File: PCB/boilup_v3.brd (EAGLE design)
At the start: 59.7 x 50.8 mm, 50 parts, among them U1 STM32F0_LQFP64, U2 SPX3819-3.3

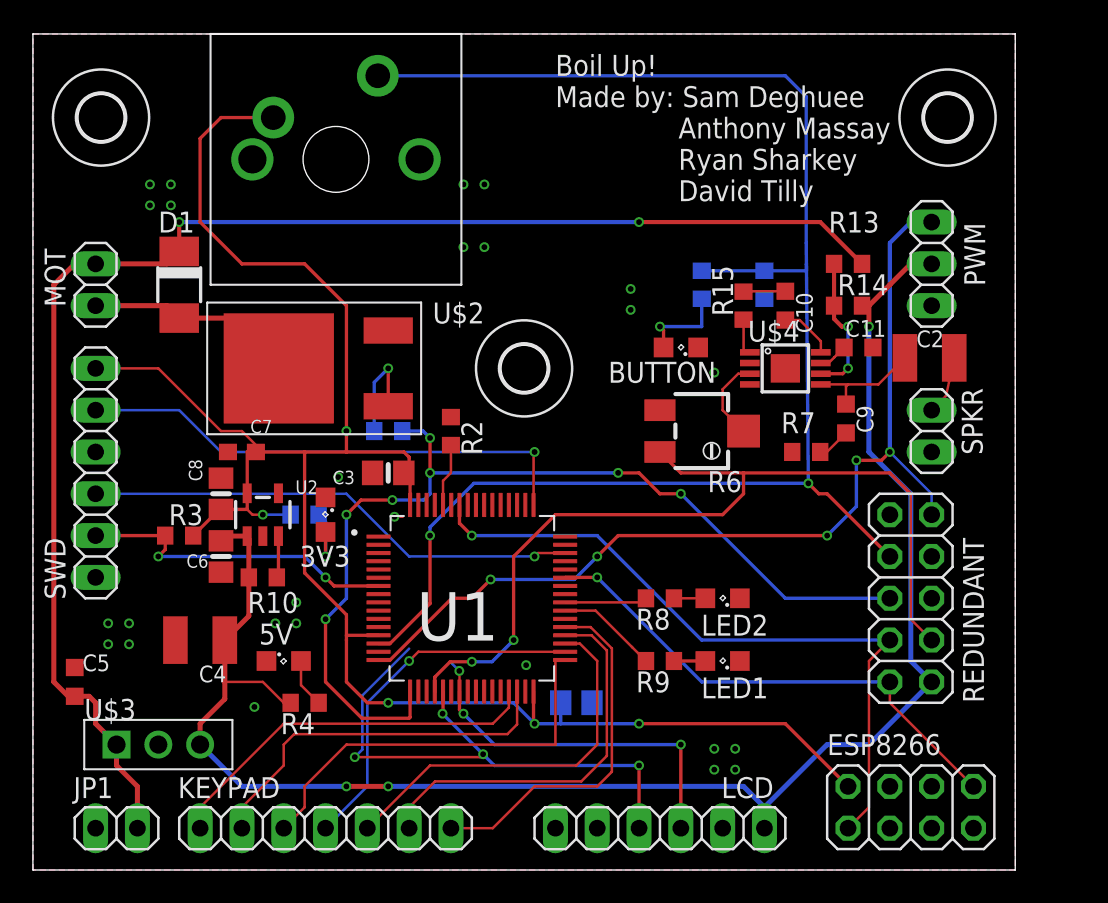
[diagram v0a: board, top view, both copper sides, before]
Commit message: v3 using i2c and a level shifter
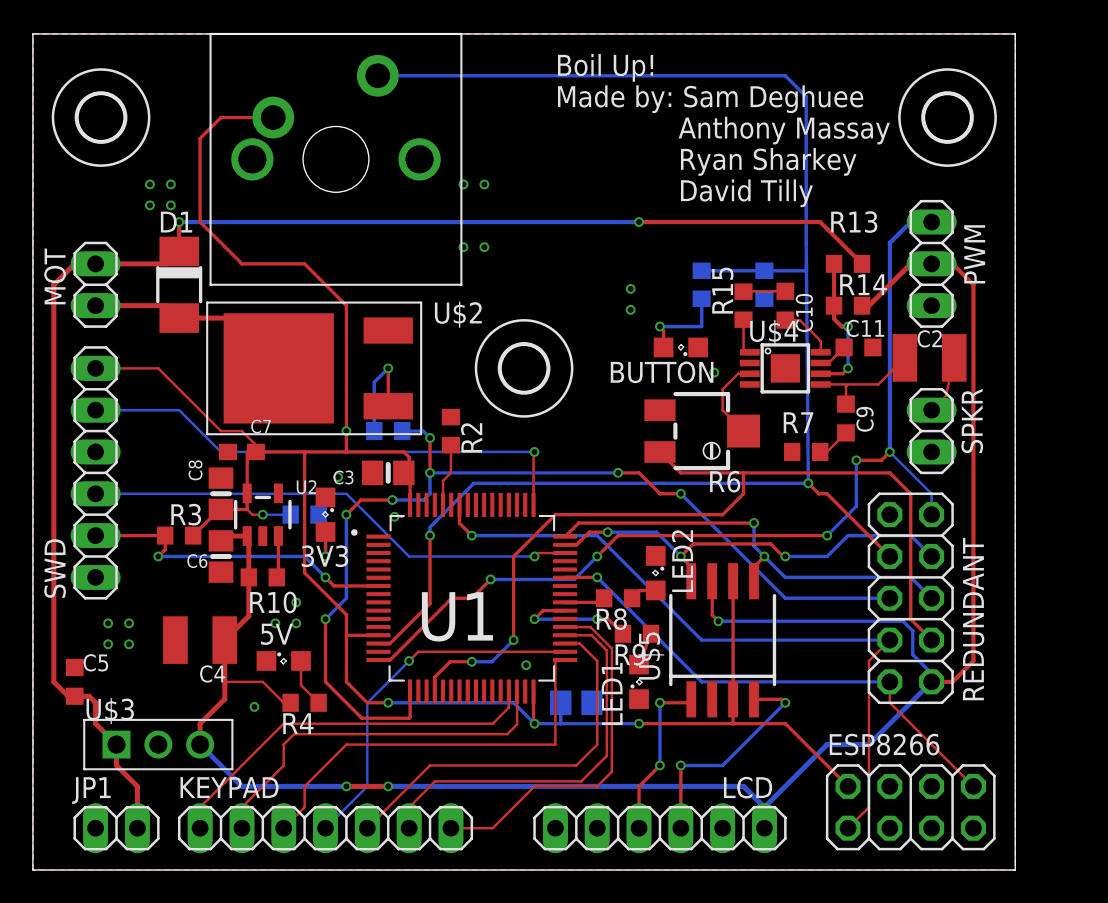
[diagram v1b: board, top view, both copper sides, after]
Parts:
- added U$5: TXS0102, smarttle:SOP-08
- moved LED1 5.24 mm to (36.8, 11.4), turned to 90 degrees
- moved LED2 4.34 mm to (37.8, 18.0), turned to 270 degrees
- moved R8 2.54 mm to (35.6, 16.5)
- moved R9 2.16 mm to (36.7, 14.4)
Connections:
- removed net MISO: U1.22
- removed net MOSI: LCD.4, U1.23
- removed net SCK: LCD.3, U1.21
- new net I2C2_SCL: REDUNDANT.7, U$5.8, U1.47
- new net I2C2_SDA: REDUNDANT.5, U$5.5, U1.48
- new net SCL: LCD.3, U$5.1
- new net SDA: LCD.4, U$5.4
- net +3V3: now also U$5.3, U$5.6
- net +5V: now also U$5.7
- net GND: now also U$5.2
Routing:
- net SCK: track 34.2 -> 0.00 mm, vias 4 -> 0
- net I2C2_SDA: track 0.00 -> 27.1 mm, vias 0 -> 2
- net I2C2_SCL: track 0.00 -> 26.7 mm, vias 0 -> 3
- net +5V: track 100.7 -> 123.5 mm
- net MOSI: track 22.5 -> 0.00 mm, vias 3 -> 0
- net SDA: track 0.00 -> 13.7 mm, vias 0 -> 2
- net SCL: track 0.00 -> 10.1 mm, vias 0 -> 2
- net +3V3: track 120.0 -> 128.7 mm
- net LED4: track 5.01 -> 2.47 mm
- net LED3: track 6.18 -> 7.82 mm, vias 0 -> 2
- net GND: vias 26 -> 22

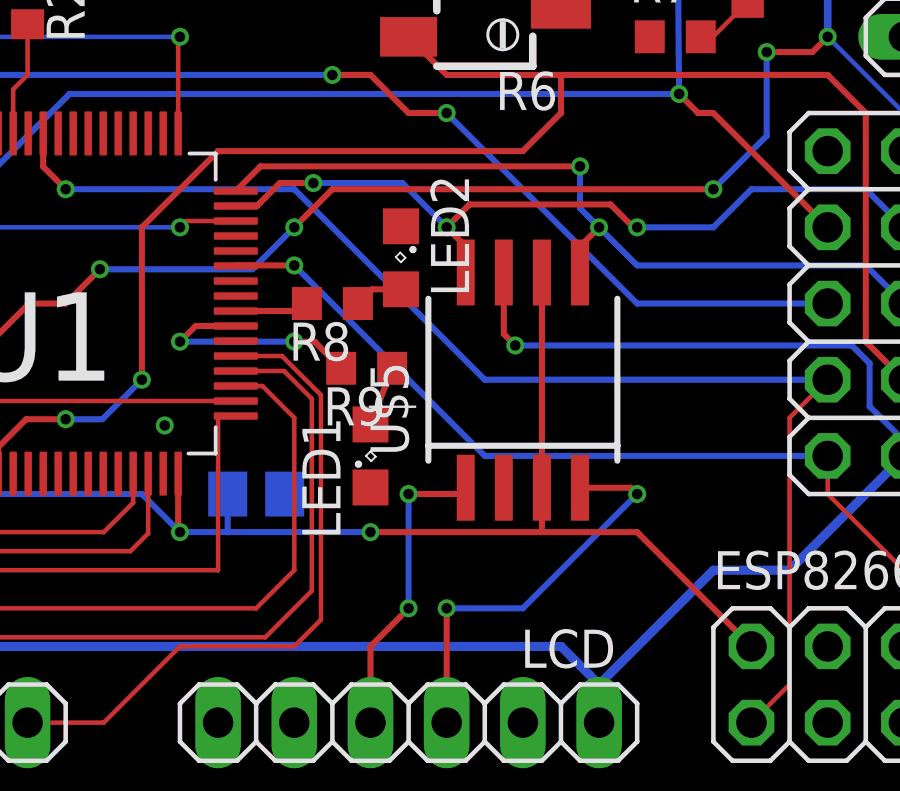
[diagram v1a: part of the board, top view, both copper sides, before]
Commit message: sam is not a smart boy, fixed logic
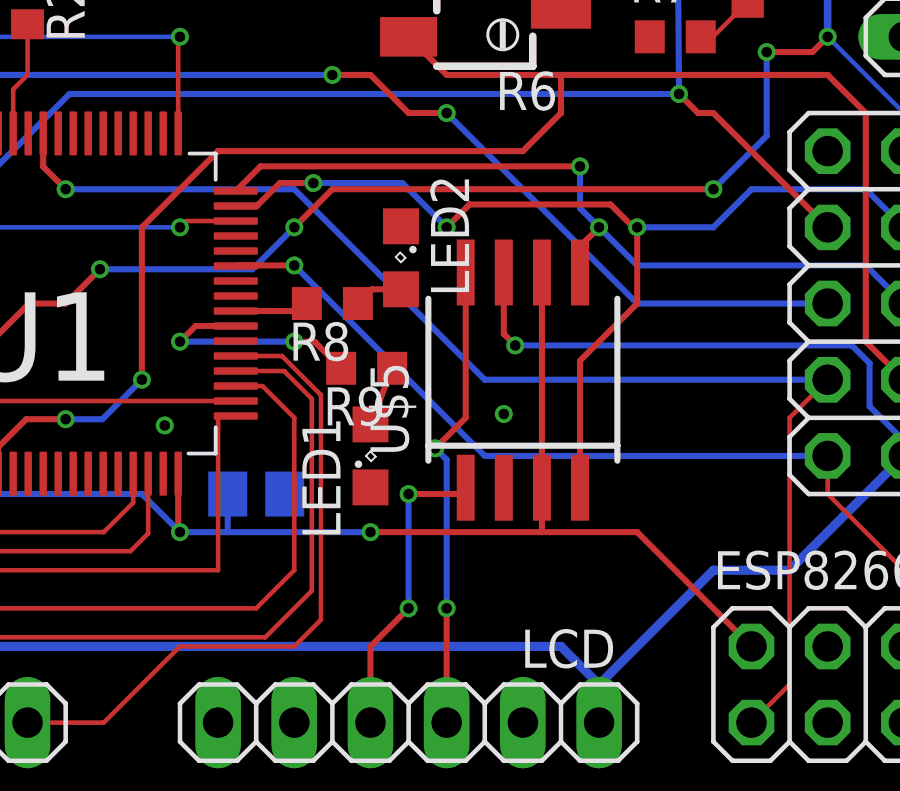
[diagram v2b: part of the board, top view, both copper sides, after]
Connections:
- net I2C2_SCL: now also U$5.4; no longer U$5.8
- net SDA: now also U$5.8; no longer U$5.4
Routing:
- net I2C2_SCL: track 26.7 -> 34.4 mm
- net SDA: track 13.7 -> 15.6 mm
- net GND: vias 22 -> 23
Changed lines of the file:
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@@
 <wire x1="22.47201875" y1="21.463" x2="21.971" y2="21.463" width="0.1524" layer="1"/>
 <contactref element="U$5" pad="2"/>
+<via x="41.275" y="12.827" extent="1-16" drill="0.35"/>
 </signal>
 <signal name="CH_PD">
@@
 <signal name="I2C2_SCL">
 <contactref element="U1" pad="47"/>
-<contactref element="U$5" pad="8"/>
 <contactref element="REDUNDANT" pad="7"/>
 <via x="34.925" y="20.526" extent="1-16" drill="0.35"/>
 <wire x1="33.80690625" y1="20.526" x2="34.925" y2="20.526" width="0.2032" layer="1"/>
-<wire x1="33.16190625" y1="19.881" x2="33.310453125" y2="20.029546875" width="0.2032" layer="1"/>
-<wire x1="33.310453125" y1="20.029546875" x2="33.80690625" y2="20.526" width="0.2032" layer="1"/>
+<wire x1="33.04090625" y1="19.76" x2="33.80690625" y2="20.526" width="0.2032" layer="1"/>
 <wire x1="34.925" y1="20.526" x2="37.894" y2="20.526" width="0.2032" layer="16"/>
 <wire x1="37.894" y1="20.526" x2="39.37" y2="19.05" width="0.2032" layer="16"/>
 <via x="39.37" y="19.05" extent="1-16" drill="0.35"/>
-<wire x1="39.37" y1="19.05" x2="40.005" y2="18.415" width="0.2032" layer="1"/>
-<wire x1="40.005" y1="18.415" x2="40.005" y2="17.545" width="0.2032" layer="1"/>
 <wire x1="54.61" y1="19.05" x2="53.34" y2="20.32" width="0.2032" layer="16"/>
 <wire x1="53.34" y1="20.32" x2="49.53" y2="20.32" width="0.2032" layer="16"/>
@@
 <wire x1="40.132" y1="19.812" x2="39.37" y2="19.05" width="0.2032" layer="1"/>
 <wire x1="32.34" y1="19.76" x2="33.04090625" y2="19.76" width="0.2032" layer="1"/>
-<wire x1="33.04090625" y1="19.76" x2="33.16190625" y2="19.881" width="0.2032" layer="1"/>
+<contactref element="U$5" pad="4"/>
+<wire x1="43.815" y1="10.37" x2="43.815" y2="14.605" width="0.2032" layer="1"/>
+<wire x1="43.815" y1="14.605" x2="45.72" y2="16.51" width="0.2032" layer="1"/>
+<wire x1="45.72" y1="16.51" x2="45.72" y2="19.05" width="0.2032" layer="1"/>
 </signal>
 <signal name="SCL">
@@
 </signal>
 <signal name="SDA">
-<contactref element="U$5" pad="4"/>
 <contactref element="LCD" pad="4"/>
 <wire x1="39.37" y1="2.54" x2="39.37" y2="6.35" width="0.2032" layer="1"/>
 <via x="39.37" y="6.35" extent="1-16" drill="0.35"/>
-<wire x1="39.37" y1="6.35" x2="41.91" y2="6.35" width="0.2032" layer="16"/>
-<wire x1="41.91" y1="6.35" x2="45.72" y2="10.16" width="0.2032" layer="16"/>
-<via x="45.72" y="10.16" extent="1-16" drill="0.35"/>
-<wire x1="45.72" y1="10.16" x2="45.51" y2="10.37" width="0.2032" layer="1"/>
-<wire x1="45.51" y1="10.37" x2="43.815" y2="10.37" width="0.2032" layer="1"/>
+<contactref element="U$5" pad="8"/>
+<wire x1="40.005" y1="17.545" x2="40.005" y2="12.7" width="0.2032" layer="1"/>
+<wire x1="40.005" y1="12.7" x2="38.989" y2="11.684" width="0.2032" layer="1"/>
+<via x="38.989" y="11.684" extent="1-16" drill="0.35"/>
+<wire x1="38.989" y1="11.684" x2="39.37" y2="11.303" width="0.2032" layer="16"/>
+<wire x1="39.37" y1="11.303" x2="39.37" y2="6.35" width="0.2032" layer="16"/>
 </signal>
 </signals>

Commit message: Final revisions and Kettle addition
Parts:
- renumbered U$2 to FET, U$3 to POWERCONV, U$4 to AMP, U$5 to LVLCONV
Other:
- board text added: "Boil Up! Made by: Sam Deghuee Anthony Massat Ryan Sharkey David Tilly"
- board text removed: "Boil Up! Made by: Sam Deghuee Anthony Massay Ryan Sharkey David Tilly"
